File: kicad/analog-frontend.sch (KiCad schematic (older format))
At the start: 17 parts, among them J1 IRON_TIP, Q1 SIA483DJ-T1-GE3, Q2 MMBT3904, U1 ACS711xEX, U2 OPA188AIDBV

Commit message: Changed out the op amp and fixed oval holes for OSHPark
I don't think I'm going to go with OSHPark. It seems they can't
fabricate this thing.
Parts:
- removed U2: OPA188AIDBV, TO_SOT_Packages_SMD:SOT-23-5, symbol OPA188AIDBV
- added C26: SPR, Capacitors_SMD:C_0402, symbol C
- added D2: BAS70-04W, TO_SOT_Packages_SMD:SOT-323_SC-70, symbol D_Schottky_x2_Serial_AKC
- added U2: MCP6V71U, TO_SOT_Packages_SMD:SOT-353_SC-70-5, symbol MCP6V71U
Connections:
- wire segments 64 -> 72
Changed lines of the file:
@@
 encoding utf-8
 Sheet 2 4
-Title ""
-Date ""
-Rev ""
-Comp ""
+Title "RT Soldering Iron"
+Date "2017-06-02"
+Rev "A"
+Comp "Kevin Cuzner"
 Comment1 ""
 Comment2 ""
@@
 $EndComp
 $Comp
-L GND #PWR01
+L GND #PWR8
 U 1 1 592A622A
 P 3400 4000
-F 0 "#PWR01" H 3400 3750 50  0001 C CNN
+F 0 "#PWR8" H 3400 3750 50  0001 C CNN
 F 1 "GND" H 3400 3850 50  0000 C CNN
 F 2 "" H 3400 4000 50  0001 C CNN
@@
 	3300 3900 3400 3900
 $Comp
-L +12V #PWR02
+L +12V #PWR2
 U 1 1 592A6425
 P 2100 1200
-F 0 "#PWR02" H 2100 1050 50  0001 C CNN
+F 0 "#PWR2" H 2100 1050 50  0001 C CNN
 F 1 "+12V" H 2100 1340 50  0000 C CNN
 F 2 "" H 2100 1200 50  0001 C CNN
@@
 Connection ~ 4300 3000
 $Comp
-L GND #PWR03
+L GND #PWR7
 U 1 1 592A6A31
 P 4300 3900
-F 0 "#PWR03" H 4300 3650 50  0001 C CNN
+F 0 "#PWR7" H 4300 3650 50  0001 C CNN
 F 1 "GND" H 4300 3750 50  0000 C CNN
 F 2 "" H 4300 3900 50  0001 C CNN
@@
 	4700 3400 4700 3300
 Connection ~ 4700 3300
-$Comp
-L OPA188AIDBV U2
-U 1 1 592BA4F6
-P 8100 4500
-F 0 "U2" H 8250 4350 60  0000 C CNN
-F 1 "OPA188AIDBV" H 8450 4650 60  0000 C CNN
-F 2 "TO_SOT_Packages_SMD:SOT-23-5" H 8100 4500 60  0001 C CNN
-F 3 "" H 8100 4500 60  0001 C CNN
-F 4 "296-36218-1-ND" H 8100 4500 60  0001 C CNN "Part No."
-	1    8100 4500
-	1    0    0    -1
-$EndComp
 Text Label 3500 3800 0    60   ~ 0
 SENSE_IN
@@
 	7800 4400 6900 4400
 $Comp
-L GND #PWR04
+L GND #PWR11
 U 1 1 592BA9A1
 P 6600 4200
-F 0 "#PWR04" H 6600 3950 50  0001 C CNN
+F 0 "#PWR11" H 6600 3950 50  0001 C CNN
 F 1 "GND" H 6600 4050 50  0000 C CNN
 F 2 "" H 6600 4200 50  0001 C CNN
@@
 	6600 4200 6600 4100
 $Comp
-L GND #PWR05
+L GND #PWR14
 U 1 1 592BA9F6
 P 8100 5000
-F 0 "#PWR05" H 8100 4750 50  0001 C CNN
+F 0 "#PWR14" H 8100 4750 50  0001 C CNN
 F 1 "GND" H 8100 4850 50  0000 C CNN
 F 2 "" H 8100 5000 50  0001 C CNN
@@
 $EndComp
 $Comp
-L +3.3VA #PWR06
+L +3.3VA #PWR10
 U 1 1 592CA321
 P 8100 4100
-F 0 "#PWR06" H 8100 3950 50  0001 C CNN
+F 0 "#PWR10" H 8100 3950 50  0001 C CNN
 F 1 "+3.3VA" H 8100 4240 50  0000 C CNN
 F 2 "" H 8100 4100 50  0001 C CNN
@@
 $EndComp
 $Comp
-L +3.3VA #PWR07
+L +3.3VA #PWR12
 U 1 1 592CA3C9
 P 8800 4800
-F 0 "#PWR07" H 8800 4650 50  0001 C CNN
+F 0 "#PWR12" H 8800 4650 50  0001 C CNN
 F 1 "+3.3VA" H 8800 4940 50  0000 C CNN
 F 2 "" H 8800 4800 50  0001 C CNN
@@
 $EndComp
 $Comp
-L GND #PWR08
+L GND #PWR17
 U 1 1 592CA3FB
 P 8800 5300
-F 0 "#PWR08" H 8800 5050 50  0001 C CNN
+F 0 "#PWR17" H 8800 5050 50  0001 C CNN
 F 1 "GND" H 8800 5150 50  0000 C CNN
 F 2 "" H 8800 5300 50  0001 C CNN
@@
 Connection ~ 5600 4600
 $Comp
-L GND #PWR09
+L GND #PWR16
 U 1 1 592CAAF6
 P 5600 5200
-F 0 "#PWR09" H 5600 4950 50  0001 C CNN
+F 0 "#PWR16" H 5600 4950 50  0001 C CNN
 F 1 "GND" H 5600 5050 50  0000 C CNN
 F 2 "" H 5600 5200 50  0001 C CNN
@@
 	5800 4100 5800 4200
 $Comp
-L +3.3VA #PWR010
+L +3.3VA #PWR9
 U 1 1 592D1E60
 P 5800 4100
-F 0 "#PWR010" H 5800 3950 50  0001 C CNN
+F 0 "#PWR9" H 5800 3950 50  0001 C CNN
 F 1 "+3.3VA" H 5800 4240 50  0000 C CNN
 F 2 "" H 5800 4100 50  0001 C CNN
@@
 Connection ~ 2100 1300
 $Comp
-L GND #PWR011
+L GND #PWR6
 U 1 1 592D5006
 P 3500 2500
-F 0 "#PWR011" H 3500 2250 50  0001 C CNN
+F 0 "#PWR6" H 3500 2250 50  0001 C CNN
 F 1 "GND" H 3500 2350 50  0000 C CNN
 F 2 "" H 3500 2500 50  0001 C CNN
@@
 Connection ~ 3500 2400
 $Comp
-L +3.3VA #PWR012
+L +3.3VA #PWR1
 U 1 1 592D518F
 P 1800 1200
-F 0 "#PWR012" H 1800 1050 50  0001 C CNN
+F 0 "#PWR1" H 1800 1050 50  0001 C CNN
 F 1 "+3.3VA" H 1800 1340 50  0000 C CNN
 F 2 "" H 1800 1200 50  0001 C CNN
@@
 $EndComp
 $Comp
-L +3.3V #PWR013
+L +3.3V #PWR4
 U 1 1 592D545D
 P 1200 2400
-F 0 "#PWR013" H 1200 2250 50  0001 C CNN
+F 0 "#PWR4" H 1200 2250 50  0001 C CNN
 F 1 "+3.3V" H 1200 2540 50  0000 C CNN
 F 2 "" H 1200 2400 50  0001 C CNN
@@
 	1800 2300 2200 2300
 $Comp
-L GND #PWR014
+L GND #PWR5
 U 1 1 592D5804
 P 2100 2500
-F 0 "#PWR014" H 2100 2250 50  0001 C CNN
+F 0 "#PWR5" H 2100 2250 50  0001 C CNN
 F 1 "GND" H 2100 2350 50  0000 C CNN
 F 2 "" H 2100 2500 50  0001 C CNN
@@
 $EndComp
 $Comp
-L GND #PWR015
+L GND #PWR15
 U 1 1 592D9ECB
 P 9400 5000
-F 0 "#PWR015" H 9400 4750 50  0001 C CNN
+F 0 "#PWR15" H 9400 4750 50  0001 C CNN
 F 1 "GND" H 9400 4850 50  0000 C CNN
 F 2 "" H 9400 5000 50  0001 C CNN
@@
 $EndComp
 $Comp
-L GND #PWR016
+L GND #PWR3
 U 1 1 592E63D8
 P 1150 1800
-F 0 "#PWR016" H 1150 1550 50  0001 C CNN
+F 0 "#PWR3" H 1150 1550 50  0001 C CNN
 F 1 "GND" H 1150 1650 50  0000 C CNN
 F 2 "" H 1150 1800 50  0001 C CNN
@@
 	1150 1300 1800 1300
 Connection ~ 1800 1300
+$Comp
+L MCP6V71U U2
+U 1 1 5930E5C8
+P 8100 4500
+F 0 "U2" H 8250 4350 60  0000 C CNN
+F 1 "MCP6V71U" H 8450 4650 60  0000 C CNN
+F 2 "TO_SOT_Packages_SMD:SOT-353_SC-70-5" H 8100 4500 60  0001 C CNN
+F 3 "" H 8100 4500 60  0001 C CNN
+F 4 "MCP6V71UT-E/LTYCT-ND" H 8100 4500 60  0001 C CNN "Part No."
+	1    8100 4500
+	1    0    0    -1
+$EndComp
+$Comp
+L D_Schottky_x2_Serial_AKC D2
+U 1 1 5930F74A
+P 4850 5300
+F 0 "D2" H 4900 5200 50  0000 C CNN
+F 1 "BAS70-04W" H 4850 5400 50  0000 C CNN
+F 2 "TO_SOT_Packages_SMD:SOT-323_SC-70" H 4850 5300 50  0001 C CNN
+F 3 "" H 4850 5300 50  0001 C CNN
+F 4 "1727-3563-1-ND" H 4850 5300 60  0001 C CNN "Part No."
+	1    4850 5300
+	0    -1   -1   0
+$EndComp
+$Comp
+L +3.3VA #PWR13
+U 1 1 5930F993
+P 4850 4900
+F 0 "#PWR13" H 4850 4750 50  0001 C CNN
+F 1 "+3.3VA" H 4850 5040 50  0000 C CNN
+F 2 "" H 4850 4900 50  0001 C CNN
+F 3 "" H 4850 4900 50  0001 C CNN
+	1    4850 4900
+	1    0    0    -1
+$EndComp
+Wire Wire Line
+	4850 4900 4850 5000
+$Comp
+L GND #PWR18
+U 1 1 5930FA31
+P 4850 5700
+F 0 "#PWR18" H 4850 5450 50  0001 C CNN
+F 1 "GND" H 4850 5550 50  0000 C CNN
+F 2 "" H 4850 5700 50  0001 C CNN
+F 3 "" H 4850 5700 50  0001 C CNN
+	1    4850 5700
+	1    0    0    -1
+$EndComp
+Wire Wire Line
+	4850 5700 4850 5600
+Wire Wire Line
+	5050 5300 5150 5300
+Wire Wire Line
+	5150 5300 5150 4600
+Connection ~ 5150 4600
+$Comp
+L C C26
+U 1 1 593100DD
+P 8100 3350
+F 0 "C26" H 8125 3450 50  0000 L CNN
+F 1 "SPR" H 8125 3250 50  0000 L CNN
+F 2 "Capacitors_SMD:C_0402" H 8138 3200 50  0001 C CNN
+F 3 "" H 8100 3350 50  0001 C CNN
+	1    8100 3350
+	0    1    1    0
+$EndComp
+Wire Wire Line
+	7950 3350 7600 3350
+Wire Wire Line
+	7600 3350 7600 3700
+Connection ~ 7600 3700
+Wire Wire Line
+	8250 3350 8400 3350
+Wire Wire Line
+	8400 3350 8400 3700
+Connection ~ 8400 3700
 $EndSCHEMATC

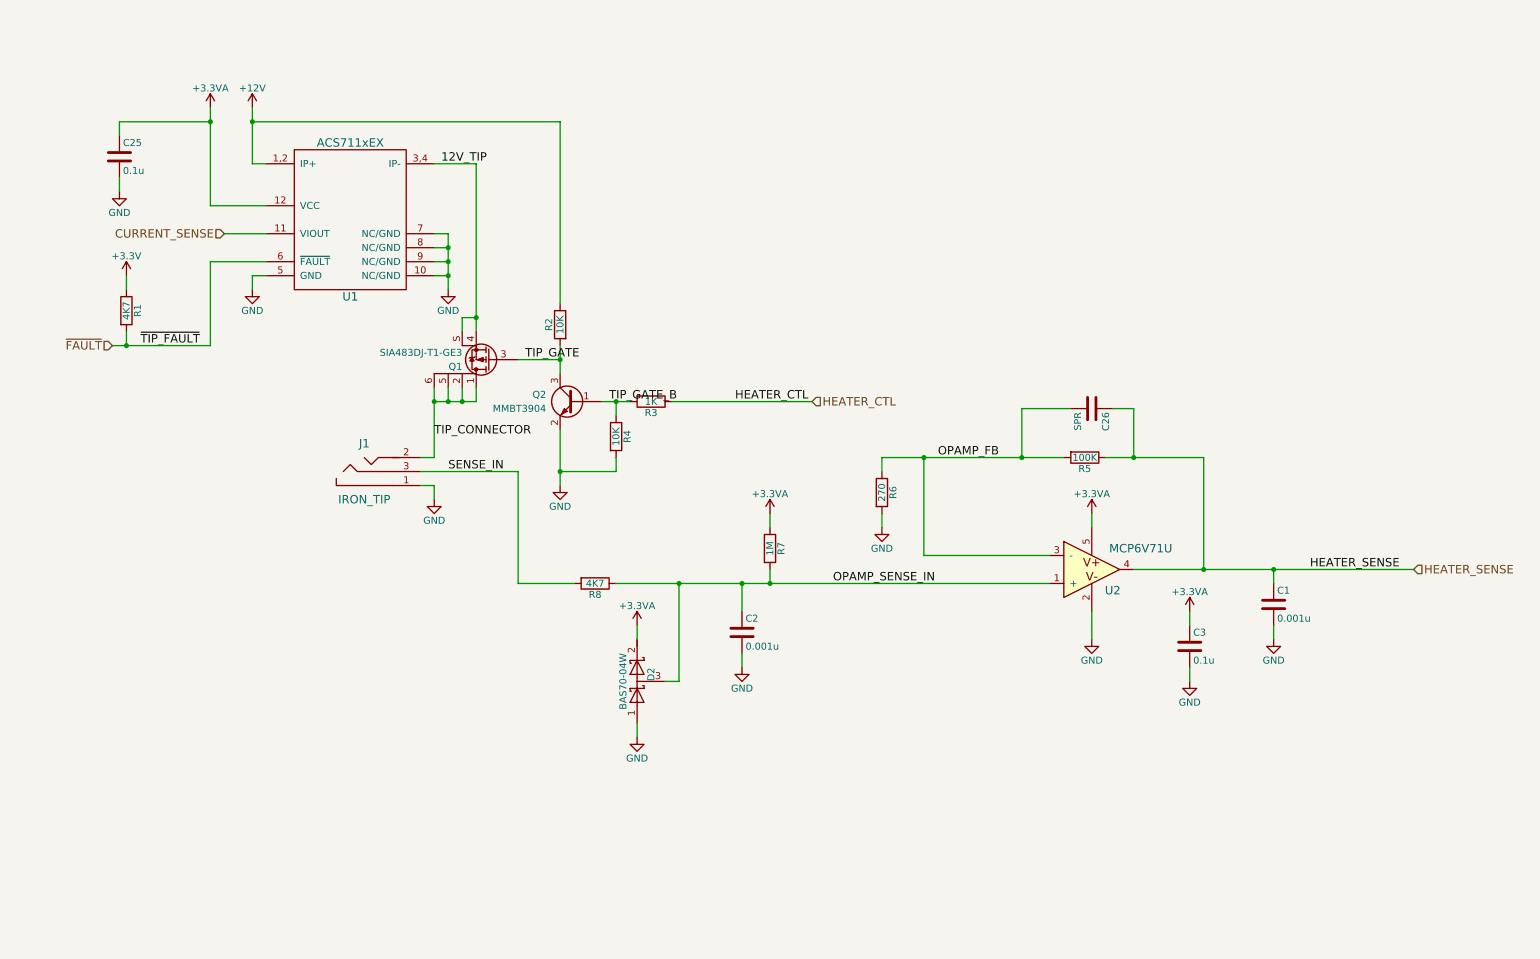
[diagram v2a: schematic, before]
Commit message: Fixed schematic to use USLetter paper
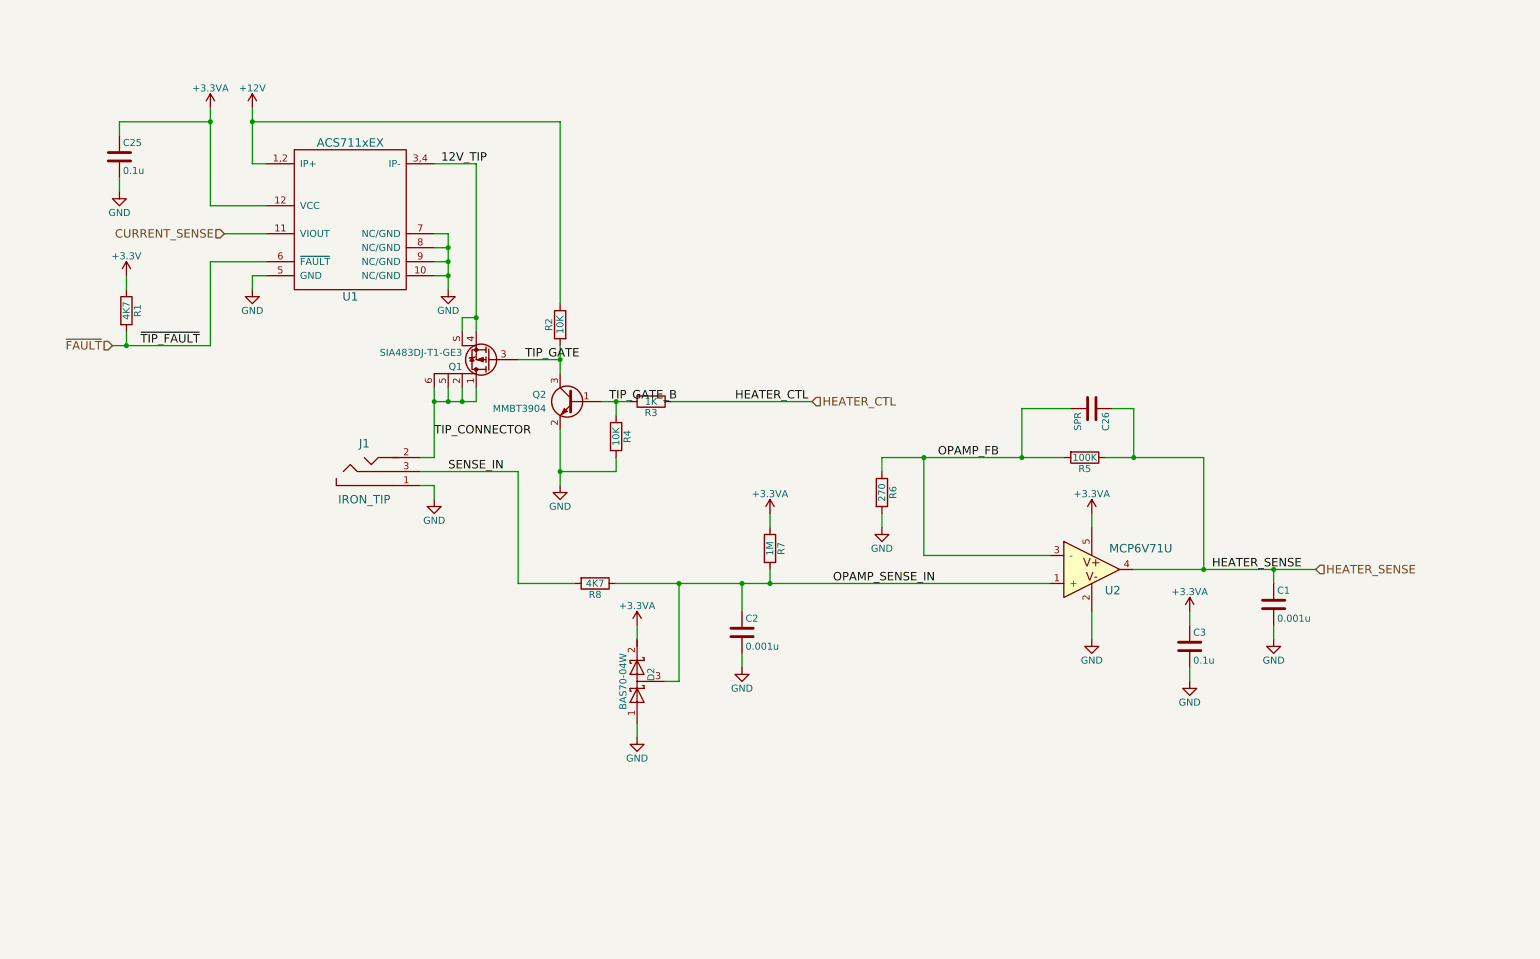
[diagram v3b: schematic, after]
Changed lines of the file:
@@
 EELAYER 25 0
 EELAYER END
-$Descr A4 11693 8268
+$Descr USLetter 11000 8500
 encoding utf-8
 Sheet 2 4
@@
 	3400 3700 3300 3700
 Wire Wire Line
-	3400 3200 3400 3700
+	3400 3200 3400 3300
+Wire Wire Line
+	3400 3300 3400 3700
 Wire Wire Line
 	3700 3300 3700 3200
 Wire Wire Line
-	3400 3300 3700 3300
+	3400 3300 3500 3300
+Wire Wire Line
+	3500 3300 3600 3300
+Wire Wire Line
+	3600 3300 3700 3300
 Connection ~ 3400 3300
 Wire Wire Line
@@
 	4300 1300 4300 2600
 Wire Wire Line
-	4300 2900 4300 3100
+	4300 2900 4300 3000
+Wire Wire Line
+	4300 3000 4300 3100
 Wire Wire Line
 	4300 3000 4000 3000
@@
 $EndComp
 Wire Wire Line
-	4300 3500 4300 3900
+	4300 3500 4300 3800
+Wire Wire Line
+	4300 3800 4300 3900
 $Comp
 L R R3
@@
 $EndComp
 Wire Wire Line
-	4600 3300 4800 3300
+	4600 3300 4700 3300
+Wire Wire Line
+	4700 3300 4800 3300
 $Comp
 L R R4
@@
 $EndComp
 Wire Wire Line
-	6600 3700 7900 3700
+	6600 3700 6900 3700
+Wire Wire Line
+	6900 3700 7600 3700
+Wire Wire Line
+	7600 3700 7900 3700
 Wire Wire Line
 	7800 4400 6900 4400
@@
 	8100 5000 8100 4800
 Wire Wire Line
-	8400 4500 10400 4500
+	8400 4500 8900 4500
+Wire Wire Line
+	8900 4500 9400 4500
+Wire Wire Line
+	9400 4500 9700 4500
 Wire Wire Line
 	8900 4500 8900 3700
 Wire Wire Line
-	8900 3700 8200 3700
-Text HLabel 10400 4500 2    60   Input ~ 0
+	8900 3700 8400 3700
+Wire Wire Line
+	8400 3700 8200 3700
+Text HLabel 9700 4500 2    60   Input ~ 0
 HEATER_SENSE
-Text Label 10300 4500 2    60   ~ 0
+Text Label 9600 4500 2    60   ~ 0
 HEATER_SENSE
 Connection ~ 8900 4500
@@
 	4000 4600 4400 4600
 Wire Wire Line
-	4700 4600 7800 4600
+	4700 4600 5150 4600
+Wire Wire Line
+	5150 4600 5600 4600
+Wire Wire Line
+	5600 4600 5800 4600
+Wire Wire Line
+	5800 4600 7800 4600
 $Comp
 L C C2
@@
 $EndComp
 Wire Wire Line
-	2100 1200 2100 1600
+	2100 1200 2100 1300
+Wire Wire Line
+	2100 1300 2100 1600
 Wire Wire Line
 	2100 1600 2200 1600
@@
 	3400 1600 3700 1600
 Wire Wire Line
-	3700 1600 3700 2800
+	3700 1600 3700 2700
+Wire Wire Line
+	3700 2700 3700 2800
 Wire Wire Line
 	3600 2700 3700 2700
@@
 $EndComp
 Wire Wire Line
-	3500 2100 3500 2500
+	3500 2100 3500 2200
+Wire Wire Line
+	3500 2200 3500 2300
+Wire Wire Line
+	3500 2300 3500 2400
+Wire Wire Line
+	3500 2400 3500 2500
 Wire Wire Line
 	3500 2100 3400 2100
@@
 $EndComp
 Wire Wire Line
-	1800 1200 1800 1900
+	1800 1200 1800 1300
+Wire Wire Line
+	1800 1300 1800 1900
 Wire Wire Line
 	1800 1900 2200 1900
@@
 	1200 2800 1200 2900
 Wire Wire Line
-	1100 2900 1800 2900
+	1100 2900 1200 2900
+Wire Wire Line
+	1200 2900 1800 2900
 Wire Wire Line
 	1800 2900 1800 2300

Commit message: Started second revision, added a comparator and eFuse
The comparator has no hysteresis in its current configuration, so that
will need to be fixed.
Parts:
- added C?: SPR, symbol C
- added R?: 33K2, symbol R
- added R?: SPR, symbol R
- added R?: 4K7, symbol R
- added R?: 49K9, Resistors_SMD:R_0402, symbol R
- added R? (x2): 10K, symbol R
- added R?: 62K, symbol R
- added U?: TPS25910, symbol TPS25910
- added U?: MCP6566, symbol MCP6566
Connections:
- net labels added: +12V_FUSED, 12V_SCALED, ~HEATER_EN
- wire segments 93 -> 116
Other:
- note added: "6A limit => 33.2K"
- note added: "8mV = 500C according to the internet\n\n8mV = 3V with 100K and 270 resistors.\n\nThe soldering iron risks damage at some very\nhot point, but most soldering happens below\n400C. Therefore, the shutoff point is going to\nbe set to somewhere just below 500C (3V)"
- note added: "Possible drop-in replacements:\nOPA333 - 296-19547-1-ND"
- moved on the sheet: C1, C2, C25, C26, C3, D2, J1, Q1, Q2, R1, R2, R3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

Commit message: Removed comp, efuse. Added zener protection. Fixed OLED footprint.
I may have destroyed a board by shorting the FB pin to ground. I left
off the zener protection on Rev A. Never again.
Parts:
- removed C?: SPR, symbol C
- removed R?: 33K2, symbol R
- removed R?: SPR, symbol R
- removed R?: 4K7, symbol R
- removed R?: 49K9, Resistors_SMD:R_0402, symbol R
- removed R? (x2): 10K, symbol R
- removed R?: 62K, symbol R
- removed U?: TPS25910, symbol TPS25910
- removed U?: MCP6566, symbol MCP6566
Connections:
- net labels removed: +12V_FUSED, 12V_SCALED, ~HEATER_EN
- wire segments 116 -> 73
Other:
- note removed: "6A limit => 33.2K"
- note removed: "8mV = 500C according to the internet\n\n8mV = 3V with 100K and 270 resistors.\n\nThe soldering iron risks damage at some very\nhot point, but most soldering happens below\n400C. Therefore, the shutoff point is going to\nbe set to somewhere just below 500C (3V)"
